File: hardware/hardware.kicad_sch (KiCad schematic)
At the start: 70 parts, among them J1 VBAT+, J10 Conn_01x05_Pin, J2 GND, J3 PHASE_A, J4 PHASE_B, J5 PHASE_C, Q1 SiR158DP, Q10 SiR158DP, Q2 SiR158DP, Q3 SiR158DP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

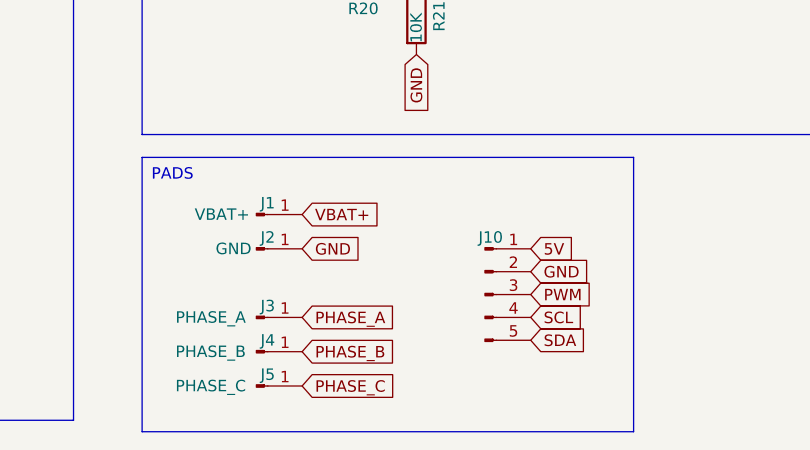
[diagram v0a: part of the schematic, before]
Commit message: additional vcc / gnd
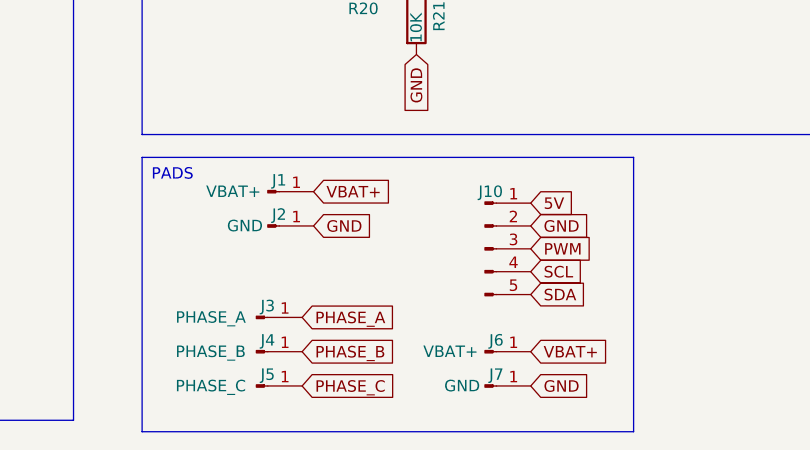
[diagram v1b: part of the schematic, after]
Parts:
- added J6: VBAT+, TestPoint:TestPoint_Pad_2.0x2.0mm, symbol Connector:Conn_01x01_Pin
- added J7: GND, TestPoint:TestPoint_Pad_2.0x2.0mm, symbol Connector:Conn_01x01_Pin
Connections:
- net GND: now also J7.1 (Pin_1)
- net VBAT+: now also J6.1 (Pin_1)
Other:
- moved on the sheet: J1, J10, J2
